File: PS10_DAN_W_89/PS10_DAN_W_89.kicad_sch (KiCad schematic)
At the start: 79 parts, among them J1 Conn_01x15_Pin, J100 Sensor_LEM, J2 IDC26, Q1 2 x BUZ11F1, Q2 2 x BUZ11F1, Q3 2 x BUZ11F1, Q4 2 x BUZ11F1, Q5 VN10KM, SW1 SW_DIP_x08, U1 AD7545, U10 LF353N, U11 LF355N, U12 LM311, U13 LM311, U14 CNX38, U14 OP77, U15 MC14584B, U16 OP77, U2 MC14585, U3 MC14585, U4 MC14013B, U5 LM399, U5 MC14013B, U6 MC14011B, U7 MC14584B, U8 OP77, U9 OP77

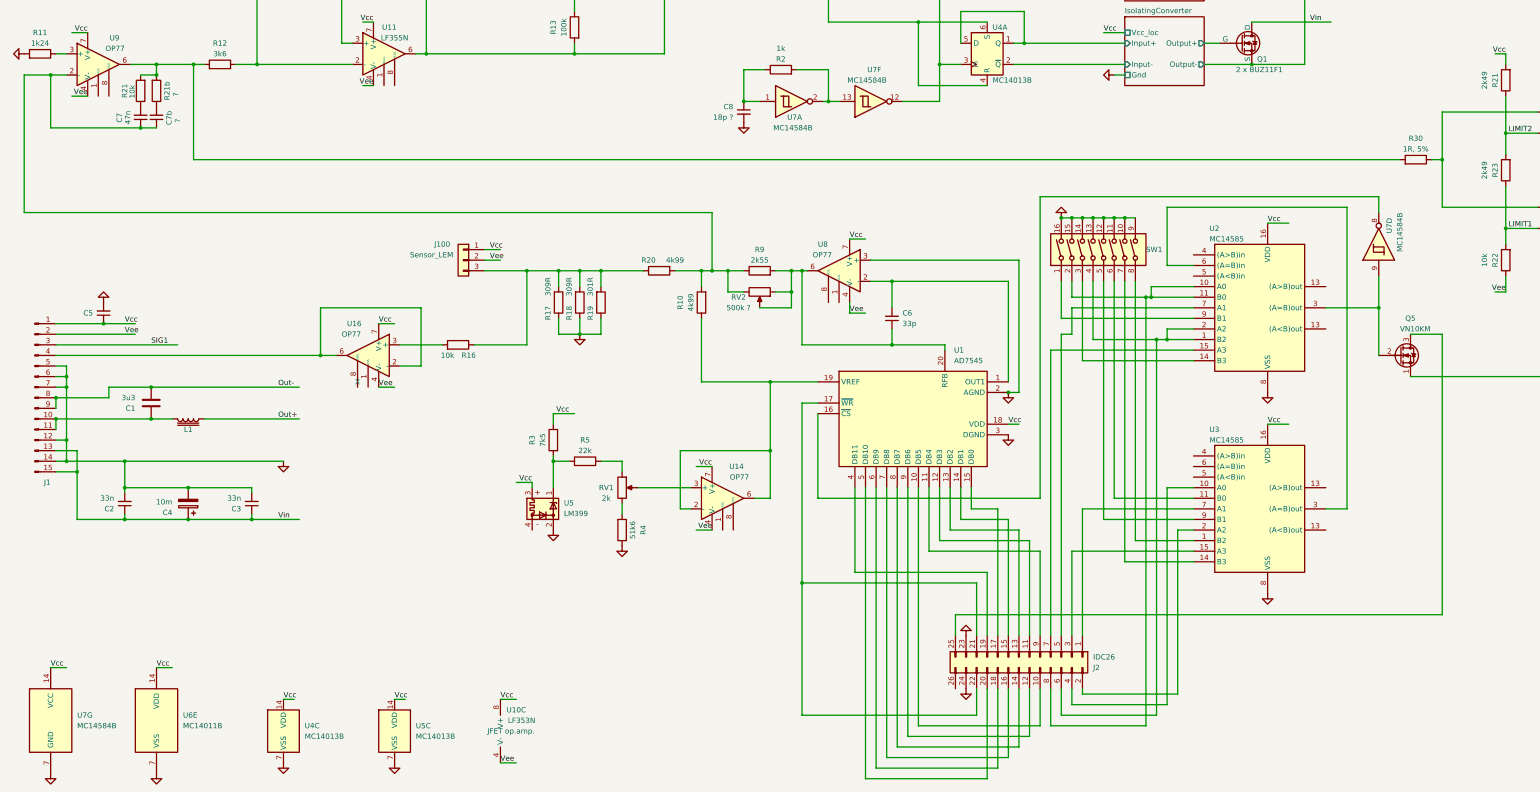
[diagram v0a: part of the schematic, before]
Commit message: Schematics corrected (resistor networks added);
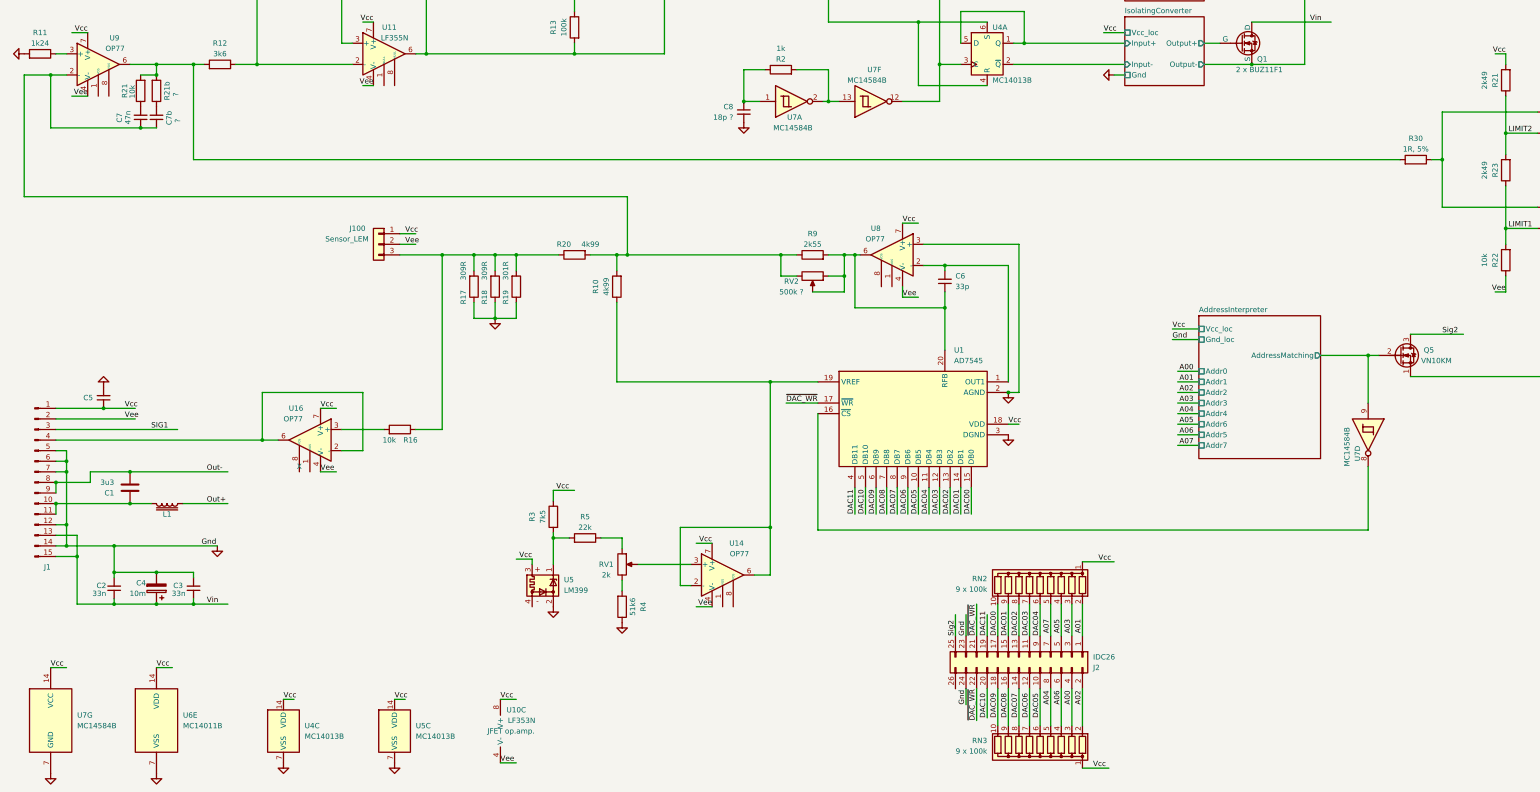
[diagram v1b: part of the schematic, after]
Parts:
- removed SW1: SW_DIP_x08, symbol Switch:SW_DIP_x08
- removed U2, U3: MC14585, symbol kpole:MC14585
- added RN2, RN3: 9 x 100k, Resistor_THT:R_Array_SIP10, symbol Device:R_Network09
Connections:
- net Vcc: now also RN2.1 (common), RN3.1 (common)
- net A06: now reaches J2.6 (Pin_6)
- net A06: now also RN3.4 (R3)
- net A04: now reaches J2.8 (Pin_8)
- net A04: now also RN3.5 (R4)
- net A07: now reaches J2.7 (Pin_7)
- net A07: now also RN2.5 (R4)
- net AddressInterpreter/AddressMatching: now reaches Q5.2 (G), U7.9
- net A05: now reaches J2.5 (Pin_5)
- net A05: now also RN2.4 (R3)
- net Sig2: now reaches J2.25 (Pin_25), Q5.3 (D)
- net DAC05: now reaches J2.10 (Pin_10), U1.10 (DB5)
- net DAC05: now also RN3.6 (R5)
- net DAC04: now reaches J2.9 (Pin_9), U1.11 (DB4)
- net DAC04: now also RN2.6 (R5)
- net DAC03: now reaches J2.11 (Pin_11), U1.12 (DB3)
- net DAC03: now also RN2.7 (R6)
- net DAC02: now reaches J2.13 (Pin_13), U1.13 (DB2)
- net DAC02: now also RN2.8 (R7)
- net DAC01: now reaches J2.15 (Pin_15), U1.14 (DB1)
- net DAC01: now also RN2.9 (R8)
- net DAC00: now reaches J2.17 (Pin_17), U1.15 (DB0)
- net DAC00: now also RN2.10 (R9)
- net ~{DAC_WR}: now reaches J2.21 (Pin_21), J2.22 (Pin_22), U1.17 (~{WR})
- net DAC11: now reaches J2.19 (Pin_19), U1.4 (DB11)
- net DAC10: now reaches J2.20 (Pin_20), U1.5 (DB10)
- net DAC09: now reaches J2.18 (Pin_18), U1.6 (DB9)
- net DAC09: now also RN3.10 (R9)
- net DAC08: now reaches J2.16 (Pin_16), U1.7 (DB8)
- net DAC08: now also RN3.9 (R8)
- net DAC07: now reaches J2.14 (Pin_14), U1.8 (DB7)
- net DAC07: now also RN3.8 (R7)
- net DAC06: now reaches J2.12 (Pin_12), U1.9 (DB6)
- net DAC06: now also RN3.7 (R6)
- net A00: now reaches J2.4 (Pin_4)
- net A00: now also RN3.3 (R2)
- net A03: now reaches J2.3 (Pin_3)
- net A03: now also RN2.3 (R2)
- net A02: now reaches J2.2 (Pin_2)
- net A02: now also RN3.2 (R1)
- net A01: now reaches J2.1 (Pin_1)
- net A01: now also RN2.2 (R1)
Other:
- added sheet AddressInterpreter (AddressInterpreter.kicad_sch)
- moved on the sheet: C1, C2, C3, C4, C5, C6, J1, J100, L1, R10, R16, R17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

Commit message: Small corrections added (3 resistors added + cosmetic corrections)
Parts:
- added C18, C21, C22, C23, C24, C25, C26, C27, C28: 100n, symbol Device:C_Small
- added C19, C20: 100u/25V, symbol Device:C_Polarized
- added R36, R37, R38: 100k, symbol Device:R
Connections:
- net DAC10: now also R36.2
- net DAC11: now also R38.1
- net GND: now also C18.1, C19.2, C20.1, C21.1, C22.1, C23.1, C24.1, C25.1, C26.1, C27.1, C28.1
- net IsolatingConverter/Input+: no longer U4.5 (D)
- net IsolatingConverter/Input-: now also U4.5 (D)
- net Vcc: now also C18.2, C19.1, C21.2, C22.2, C23.2, C24.2, C25.2, C26.2, C27.2, C28.2, R36.1, R37.2, R38.2
- net Vee: now also C20.2
- net ~{DAC_WR}: now also R37.1
- net Vin renamed Vpwr
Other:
- moved on the sheet: R3, R4, R5, RV1, U10C, U14, U4C, U5, U5C, U6E

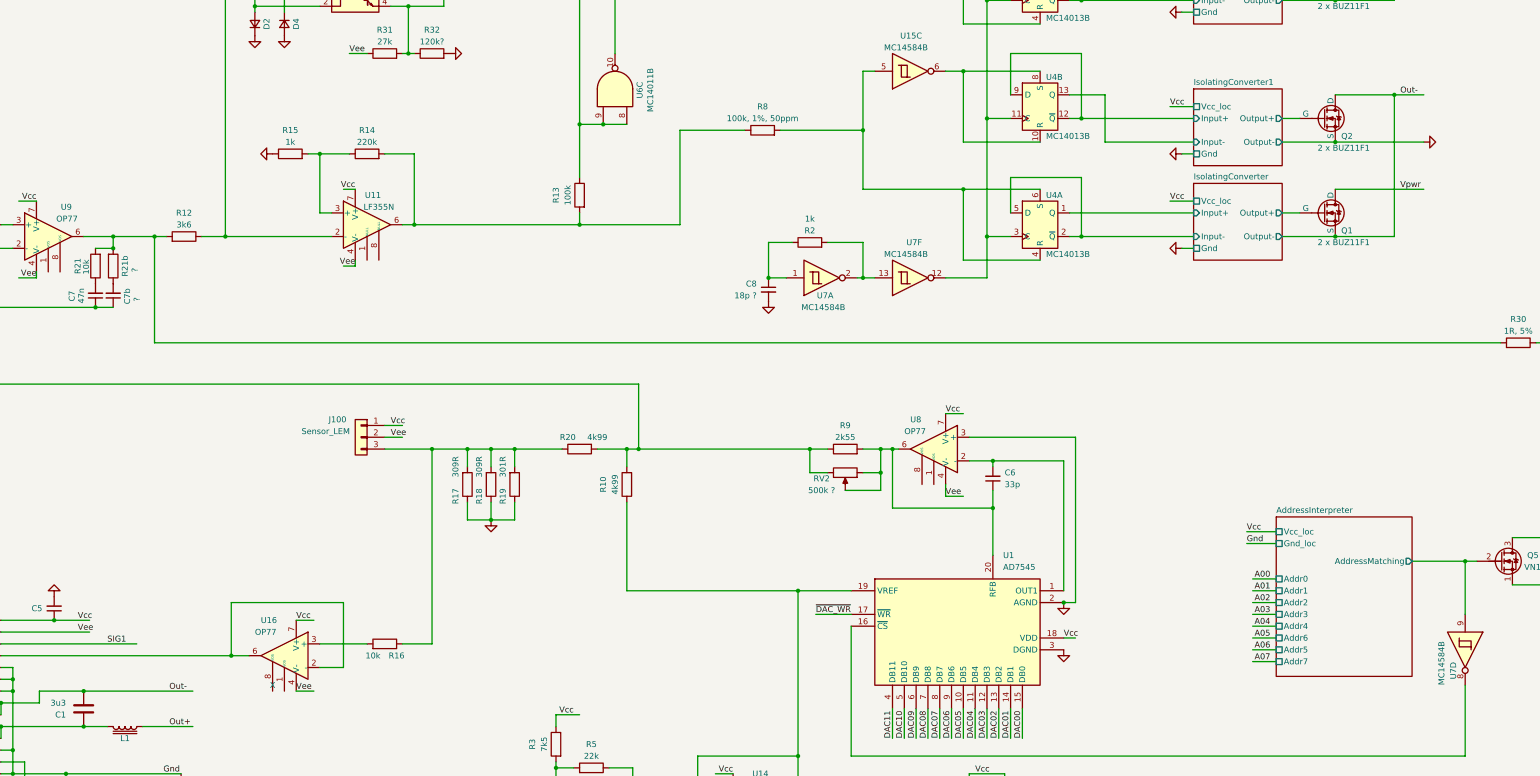
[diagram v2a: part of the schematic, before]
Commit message: Some bugs fixed (U4A.D = U4A./Q; 3 pull-up resistors added; L2 winding added);
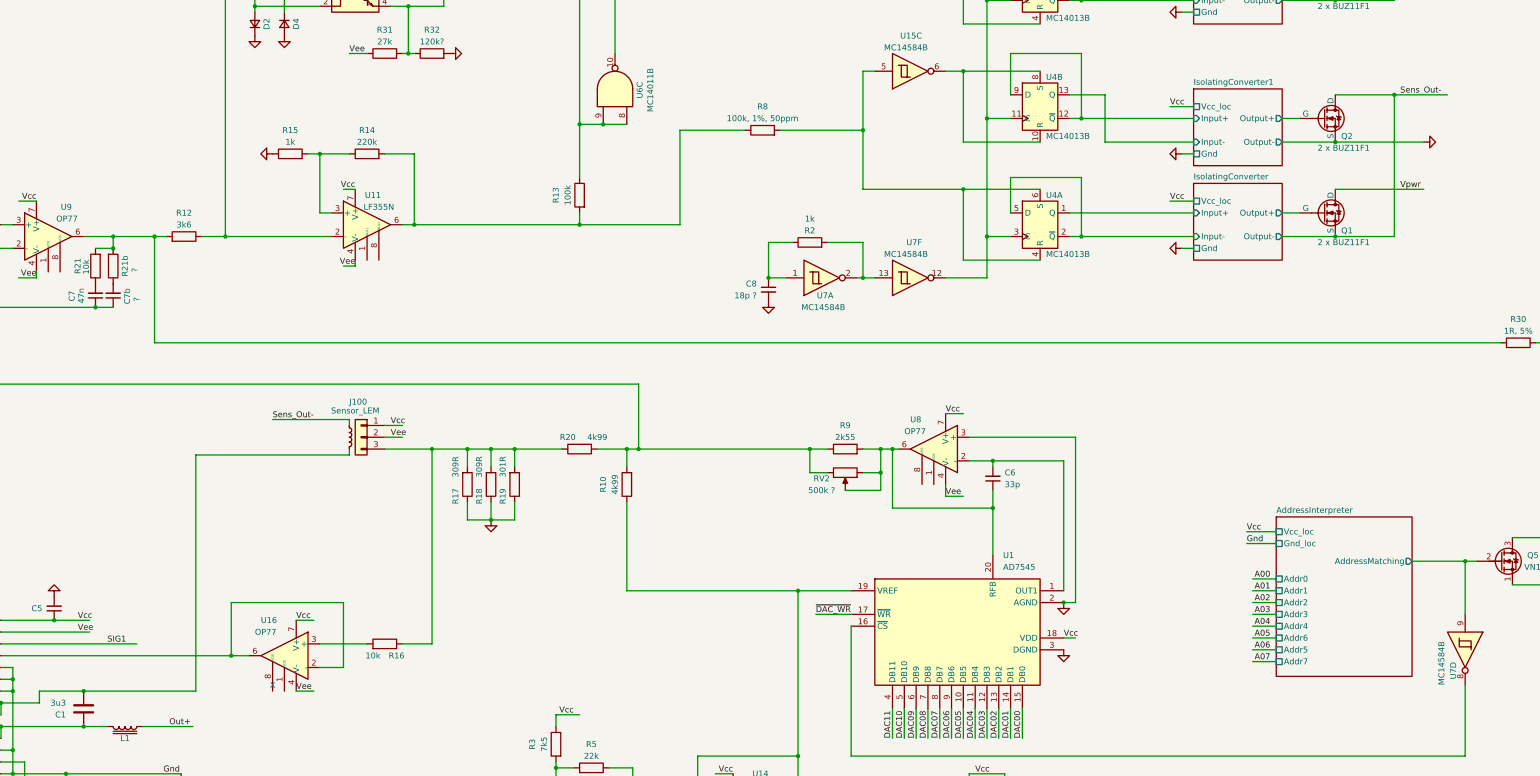
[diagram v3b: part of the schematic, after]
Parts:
- added L2: L_Small, symbol Device:L_Small
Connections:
- net Out-: no longer names the net of C1.2, J1.8 (Pin_8), J1.9 (Pin_9)
- net Out-: now also L2.2; no longer Q1.3 (S), Q2.1 (D)
- new net Sens_Out-: L2.1, Q1.3 (S), Q2.1 (D)
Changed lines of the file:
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@@
     (stroke (width 0) (type default))
   )
+  (wire (pts (xy 101.6 154.94) (xy 101.6 156.21))
+    (stroke (width 0) (type default))
+  )
   (wire (pts (xy 40.64 224.79) (xy 65.405 224.79))
     (stroke (width 0) (type default))
@@
     (stroke (width 0) (type default))
   )
+  (wire (pts (xy 68.58 156.21) (xy 68.58 207.01))
+    (stroke (width 0) (type default))
+  )
   (wire (pts (xy 243.84 69.85) (xy 259.08 69.85))
     (stroke (width 0) (type default))
@@
     (stroke (width 0) (type default))
   )
+  (wire (pts (xy 85.09 148.59) (xy 101.6 148.59))
+    (stroke (width 0) (type default))
+  )
   (wire (pts (xy 29.21 201.93) (xy 26.67 201.93))
     (stroke (width 0) (type default))
@@
     (stroke (width 0) (type default))
   )
-  (wire (pts (xy 326.39 78.74) (xy 332.74 78.74))
+  (wire (pts (xy 326.39 78.74) (xy 337.82 78.74))
     (stroke (width 0) (type default))
   )
@@
     (stroke (width 0) (type default))
   )
+  (wire (pts (xy 101.6 156.21) (xy 68.58 156.21))
+    (stroke (width 0) (type default))
+  )
   (wire (pts (xy 238.76 118.11) (xy 229.87 118.11))
     (stroke (width 0) (type default))
@@
     (stroke (width 0) (type default))
   )
-  (wire (pts (xy 44.45 207.01) (xy 67.945 207.01))
+  (wire (pts (xy 44.45 207.01) (xy 68.58 207.01))
     (stroke (width 0) (type default))
   )
@@
     (stroke (width 0) (type default))
   )
+  (wire (pts (xy 101.6 148.59) (xy 101.6 149.86))
+    (stroke (width 0) (type default))
+  )
   (wire (pts (xy 215.9 160.02) (xy 215.9 154.94))
     (stroke (width 0) (type default))
@@
     (effects (font (size 1.27 1.27)) (justify right bottom))
   )
-  (label "Out-" (at 327.66 78.74 0) (fields_autoplaced)
+  (label "Sens_Out-" (at 327.66 78.74 0) (fields_autoplaced)
     (effects (font (size 1.27 1.27)) (justify left bottom))
   )
@@
     (effects (font (size 1.27 1.27)) (justify left bottom))
   )
-  (label "Out-" (at 62.865 207.01 0) (fields_autoplaced)
+  (label "Sens_Out-" (at 85.09 148.59 0) (fields_autoplaced)
     (effects (font (size 1.27 1.27)) (justify left bottom))
   )
@@
     )
   )
+  (symbol (lib_id "Device:L_Small") (at 101.6 152.4 0) (unit 1)
+    (in_bom yes) (on_board yes) (dnp no)
+    (property "Reference" "L2" (at 98.425 152.4 0)
+      (effects (font (size 1.27 1.27)) (justify left) hide)
+    )
+    (property "Value" "L_Small" (at 92.075 153.035 0)
+      (effects (font (size 1.27 1.27)) (justify left) hide)
+    )
+    (property "Footprint" "" (at 101.6 152.4 0)
+      (effects (font (size 1.27 1.27)) hide)
+    )
+    (property "Datasheet" "~" (at 101.6 152.4 0)
+      (effects (font (size 1.27 1.27)) hide)
+    )
+    (pin "2")
+    (pin "1")
+    (instances
+      (project "PS10_DAN_W_89"
+        (path "/e91a2aa5-4be5-4ade-bc4c-021deb2b0b30"
+          (reference "L2") (unit 1)
+        )
+      )
+    )
+  )
   (symbol (lib_id "Device:R") (at 46.99 115.57 180) (unit 1)
     (in_bom yes) (on_board yes) (dnp no)
@@
   (symbol (lib_id "Connector_Generic:Conn_01x03") (at 104.14 152.4 0) (mirror y) (unit 1)
     (in_bom yes) (on_board yes) (dnp no)
-    (property "Reference" "J100" (at 99.06 148.59 0)
+    (property "Reference" "J100" (at 103.505 144.78 0)
       (effects (font (size 1.27 1.27)))
     )
-    (property "Value" "Sensor_LEM" (at 96.52 151.13 0)
+    (property "Value" "Sensor_LEM" (at 102.87 146.685 0)
       (effects (font (size 1.27 1.27)))
     )
